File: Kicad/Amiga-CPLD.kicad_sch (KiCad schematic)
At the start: 23 parts, among them CN1 CDTV-DIAG, J1 Conn_01x06_Male, U1 AZ1117-3.3, U2 XC95144XL-TQ100, X1 50MHz

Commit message: PCB: Keep on routing...
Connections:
- net IORDY: now also U2.4 (I/O/GTS2)
- net ~{FLASH_CE}: now also U2.97 (P97)
- net ~{IDE_CS1}: now also U2.2 (I/O/GTS4)
- net ~{IDE_ROMCS}: now also U2.1 (I/O/GTS3)
- net ~{IORD}: now also U2.96 (P96)
- net ~{IOWR}: now also U2.99 (I/O/GSR)
- net ~{I_BUFOE}: now also U2.6 (P6)
- net ~{IDE_CS2}: now reaches U2.3 (I/O/GTS1)
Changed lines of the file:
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@@
   (junction (at 86.995 180.34) (diameter 1.016) (color 0 0 0 0)
   )
-  (no_connect (at 185.42 25.4))
+  (no_connect (at 213.995 32.385))
   (no_connect (at 40.005 39.37))
   (no_connect (at 40.005 44.45))
@@
     (stroke (width 0) (type default) (color 0 0 0 0))
   )
+  (wire (pts (xy 133.35 72.39) (xy 125.095 72.39))
+    (stroke (width 0) (type default) (color 0 0 0 0))
+  )
   (wire (pts (xy 153.67 24.13) (xy 156.21 24.13))
     (stroke (width 0) (type solid) (color 0 0 0 0))
@@
     (stroke (width 0) (type default) (color 0 0 0 0))
   )
-  (wire (pts (xy 249.555 128.27) (xy 257.81 128.27))
-    (stroke (width 0) (type default) (color 0 0 0 0))
-  )
   (wire (pts (xy 81.915 49.53) (xy 86.995 49.53))
     (stroke (width 0) (type default) (color 0 0 0 0))
@@
     (stroke (width 0) (type default) (color 0 0 0 0))
   )
-  (wire (pts (xy 249.555 123.19) (xy 257.81 123.19))
+  (wire (pts (xy 133.35 138.43) (xy 125.095 138.43))
     (stroke (width 0) (type default) (color 0 0 0 0))
   )
@@
     (stroke (width 0) (type default) (color 0 0 0 0))
   )
-  (wire (pts (xy 208.28 27.94) (xy 215.9 27.94))
-    (stroke (width 0) (type default) (color 0 0 0 0))
-  )
   (bus (pts (xy 89.535 69.85) (xy 89.535 72.39))
     (stroke (width 0) (type default) (color 0 0 0 0))
@@
     (stroke (width 0) (type default) (color 0 0 0 0))
   )
-  (wire (pts (xy 249.555 107.95) (xy 257.81 107.95))
+  (wire (pts (xy 133.35 67.31) (xy 125.095 67.31))
     (stroke (width 0) (type default) (color 0 0 0 0))
   )
@@
     (stroke (width 0) (type solid) (color 0 0 0 0))
   )
-  (wire (pts (xy 208.28 20.32) (xy 215.9 20.32))
+  (wire (pts (xy 133.35 140.97) (xy 125.73 140.97))
     (stroke (width 0) (type default) (color 0 0 0 0))
   )
@@
     (stroke (width 0) (type default) (color 0 0 0 0))
   )
-  (wire (pts (xy 249.555 120.65) (xy 257.81 120.65))
+  (wire (pts (xy 133.35 62.23) (xy 125.095 62.23))
     (stroke (width 0) (type default) (color 0 0 0 0))
   )
@@
     (stroke (width 0) (type solid) (color 0 0 0 0))
   )
-  (wire (pts (xy 208.28 17.78) (xy 215.9 17.78))
+  (wire (pts (xy 133.35 64.77) (xy 125.73 64.77))
     (stroke (width 0) (type default) (color 0 0 0 0))
   )
@@
     (stroke (width 0) (type solid) (color 0 0 0 0))
   )
-  (wire (pts (xy 249.555 125.73) (xy 257.81 125.73))
+  (wire (pts (xy 133.35 74.93) (xy 125.095 74.93))
     (stroke (width 0) (type default) (color 0 0 0 0))
   )
@@
     (stroke (width 0) (type solid) (color 0 0 0 0))
   )
-  (wire (pts (xy 249.555 118.11) (xy 257.81 118.11))
-    (stroke (width 0) (type default) (color 0 0 0 0))
-  )
   (wire (pts (xy 113.665 180.34) (xy 122.555 180.34))
     (stroke (width 0) (type solid) (color 0 0 0 0))
@@
     (stroke (width 0) (type solid) (color 0 0 0 0))
   )
-  (wire (pts (xy 208.28 22.86) (xy 215.9 22.86))
-    (stroke (width 0) (type default) (color 0 0 0 0))
-  )
   (wire (pts (xy 29.845 105.41) (xy 40.005 105.41))
     (stroke (width 0) (type default) (color 0 0 0 0))
@@
     (stroke (width 0) (type solid) (color 0 0 0 0))
   )
-  (wire (pts (xy 249.555 110.49) (xy 257.81 110.49))
+  (wire (pts (xy 133.35 69.85) (xy 125.095 69.85))
     (stroke (width 0) (type default) (color 0 0 0 0))
   )
@@
     (effects (font (size 1.27 1.27)) (justify right bottom))
   )
-  (label "~{BGACK}" (at 185.42 15.24 0)
-    (effects (font (size 1.27 1.27)) (justify left bottom))
-  )
   (label "MA9" (at 184.15 31.75 0)
     (effects (font (size 1.27 1.27)) (justify left bottom))
@@
     (effects (font (size 1.27 1.27)) (justify right bottom))
   )
-  (label "~{IDE_CS2}" (at 249.555 107.95 0)
-    (effects (font (size 1.27 1.27)) (justify left bottom))
+  (label "~{IDE_CS2}" (at 133.35 69.85 180)
+    (effects (font (size 1.27 1.27)) (justify right bottom))
   )
   (label "CKE" (at 133.35 100.33 180)
@@
     (effects (font (size 1.27 1.27)) (justify left bottom))
   )
-  (label "RAM_J1" (at 185.42 27.94 0)
+  (label "RAM_J1" (at 212.725 38.1 0)
     (effects (font (size 1.27 1.27)) (justify left bottom))
   )
@@
     (effects (font (size 1.27 1.27)) (justify left bottom))
   )
-  (label "~{IOWR}" (at 249.555 120.65 0)
-    (effects (font (size 1.27 1.27)) (justify left bottom))
+  (label "~{IOWR}" (at 133.35 62.23 180)
+    (effects (font (size 1.27 1.27)) (justify right bottom))
   )
   (label "D6" (at 81.915 102.87 0)
@@
     (effects (font (size 1.27 1.27)) (justify right bottom))
   )
-  (label "~{IDE_IRQ}" (at 249.555 128.27 0)
-    (effects (font (size 1.27 1.27)) (justify left bottom))
-  )
   (label "DQML" (at 130.81 36.83 180)
     (effects (font (size 1.27 1.27)) (justify right bottom))
@@
     (effects (font (size 1.27 1.27)) (justify left bottom))
   )
-  (label "~{INT2}" (at 185.42 17.78 0)
-    (effects (font (size 1.27 1.27)) (justify left bottom))
-  )
   (label "~{AS}" (at 184.15 95.25 0)
     (effects (font (size 1.27 1.27)) (justify left bottom))
@@
     (effects (font (size 1.27 1.27)) (justify left bottom))
   )
-  (label "~{IORD}" (at 249.555 123.19 0)
-    (effects (font (size 1.27 1.27)) (justify left bottom))
+  (label "~{IORD}" (at 133.35 138.43 180)
+    (effects (font (size 1.27 1.27)) (justify right bottom))
   )
   (label "MA11" (at 133.35 110.49 180)
@@
     (effects (font (size 1.27 1.27)) (justify right bottom))
   )
-  (label "IORDY" (at 249.555 125.73 0)
-    (effects (font (size 1.27 1.27)) (justify left bottom))
+  (label "IORDY" (at 133.35 72.39 180)
+    (effects (font (size 1.27 1.27)) (justify right bottom))
   )
   (label "TMS" (at 184.15 148.59 0)
@@
     (effects (font (size 1.27 1.27)) (justify left bottom))
   )
+  (label "~{I_BUFOE}" (at 133.35 74.93 180)
+    (effects (font (size 1.27 1.27)) (justify right bottom))
+  )
   (label "A4" (at 133.35 118.11 180)
     (effects (font (size 1.27 1.27)) (justify right bottom))
@@
     (effects (font (size 1.27 1.27)) (justify left bottom))
   )
-  (label "~{I_BUFOE}" (at 249.555 118.11 0)
-    (effects (font (size 1.27 1.27)) (justify left bottom))
-  )
   (label "D12" (at 184.15 107.95 0)
     (effects (font (size 1.27 1.27)) (justify left bottom))
@@
     (effects (font (size 1.27 1.27)) (justify left bottom))
   )
-  (label "~{IDE_CS1}" (at 249.555 110.49 0)
-    (effects (font (size 1.27 1.27)) (justify left bottom))
+  (label "~{IDE_CS1}" (at 133.35 67.31 180)
+    (effects (font (size 1.27 1.27)) (justify right bottom))
   )
   (label "D13" (at 184.15 105.41 0)
@@
     )
   )
+  (hierarchical_label "~{I_BUFOE}" (shape output) (at 125.095 74.93 180)
+    (effects (font (size 1.27 1.27)) (justify right))
+  )
   (hierarchical_label "BA1" (shape output) (at 125.095 113.03 180)
     (effects (font (size 1.27 1.27)) (justify right))
@@
     (effects (font (size 1.27 1.27)) (justify right))
   )
-  (hierarchical_label "~{FLASH_BSY}" (shape input) (at 215.9 27.94 0)
-    (effects (font (size 1.27 1.27)) (justify left))
-  )
   (hierarchical_label "~{R_BUFOE}" (shape output) (at 193.675 12.7 0)
     (effects (font (size 1.27 1.27)) (justify left))
@@
     (effects (font (size 1.27 1.27)) (justify left))
   )
-  (hierarchical_label "FLASH_A18" (shape output) (at 215.9 22.86 0)
-    (effects (font (size 1.27 1.27)) (justify left))
-  )
-  (hierarchical_label "~{IDE_CS1}" (shape output) (at 257.81 107.95 0)
-    (effects (font (size 1.27 1.27)) (justify left))
+  (hierarchical_label "~{IDE_CS1}" (shape output) (at 125.095 67.31 180)
+    (effects (font (size 1.27 1.27)) (justify right))
   )
   (hierarchical_label "~{CAS}" (shape output) (at 122.555 41.91 180)
     (effects (font (size 1.27 1.27)) (justify right))
   )
-  (hierarchical_label "~{I_BUFOE}" (shape output) (at 257.81 118.11 0)
-    (effects (font (size 1.27 1.27)) (justify left))
-  )
   (hierarchical_label "RAM_~{W}" (shape output) (at 122.555 39.37 180)
     (effects (font (size 1.27 1.27)) (justify right))
   )
-  (hierarchical_label "~{IDE_ROMCS}" (shape output) (at 215.9 17.78 0)
-    (effects (font (size 1.27 1.27)) (justify left))
+  (hierarchical_label "~{IDE_ROMCS}" (shape output) (at 125.73 64.77 180)
+    (effects (font (size 1.27 1.27)) (justify right))
   )
   (hierarchical_label "MA[0..11]" (shape output) (at 264.795 23.495 0)
     (effects (font (size 1.27 1.27)) (justify left))
   )
-  (hierarchical_label "~{FLASH_CE}" (shape output) (at 215.9 20.32 0)
-    (effects (font (size 1.27 1.27)) (justify left))
-  )
-  (hierarchical_label "~{IDE_IRQ}" (shape input) (at 257.81 128.27 0)
-    (effects (font (size 1.27 1.27)) (justify left))
+  (hierarchical_label "~{FLASH_CE}" (shape output) (at 125.73 140.97 180)
+    (effects (font (size 1.27 1.27)) (justify right))
   )
   (hierarchical_label "CKE" (shape output) (at 125.095 100.33 180)
     (effects (font (size 1.27 1.27)) (justify right))
   )
-  (hierarchical_label "~{IDE_CS2}" (shape output) (at 257.81 110.49 0)
-    (effects (font (size 1.27 1.27)) (justify left))
-  )
-  (hierarchical_label "~{IORD}" (shape output) (at 257.81 123.19 0)
-    (effects (font (size 1.27 1.27)) (justify left))
-  )
-  (hierarchical_label "IORDY" (shape input) (at 257.81 125.73 0)
-    (effects (font (size 1.27 1.27)) (justify left))
-  )
-  (hierarchical_label "~{IOWR}" (shape output) (at 257.81 120.65 0)
-    (effects (font (size 1.27 1.27)) (justify left))
+  (hierarchical_label "~{IDE_CS2}" (shape output) (at 125.095 69.85 180)
+    (effects (font (size 1.27 1.27)) (justify right))
+  )
+  (hierarchical_label "~{IORD}" (shape output) (at 125.095 138.43 180)
+    (effects (font (size 1.27 1.27)) (justify right))
+  )
+  (hierarchical_label "IORDY" (shape input) (at 125.095 72.39 180)
+    (effects (font (size 1.27 1.27)) (justify right))
+  )
+  (hierarchical_label "~{IOWR}" (shape output) (at 125.095 62.23 180)
+    (effects (font (size 1.27 1.27)) (justify right))
   )
   (hierarchical_label "BA0" (shape output) (at 125.095 107.95 180)

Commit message: PCB: More routing...
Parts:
- removed JP2: configure_ram, Connector_PinHeader_2.54mm:PinHeader_1x02_P2.54mm_Vertical, symbol Connector:Conn_01x02_Male
- removed R3: 10k, Resistor_SMD:R_0603_1608Metric, symbol Device:R
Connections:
- net BA0: now also U2.29 (P29); no longer U2.32 (P32)
- net BA1: now also U2.32 (P32); no longer U2.34 (P34)
- net CKE: now also U2.27 (I/O/GCK3); no longer U2.28 (P28)
- net DQMH: now also U2.22 (I/O/GCK1)
- net DQML: now also U2.19 (P19)
- net MA0: now also U2.36 (P36); no longer U2.39 (P39)
- net MA1: now also U2.39 (P39); no longer U2.41 (P41)
- net MA10: now also U2.34 (P34); no longer U2.36 (P36)
- net MA11: now also U2.30 (P30); no longer U2.33 (P33)
- net MA2: now also U2.41 (P41); no longer U2.43 (P43)
- net MA3: now also U2.43 (P43); no longer U2.49 (P49)
- net MA8: now also U2.35 (P35); no longer U2.50 (P50)
- net MA9: now also U2.33 (P33); no longer U2.35 (P35)
- net MEMCLK: now also U2.23 (I/O/GCK2); no longer U2.27 (I/O/GCK3)
- net RAM_J1: now also JP3.1 (Pin_1), U2.49 (P49)
- net RAM_~{W}: now also U2.20 (P20)
- net ~{CAS}: now also U2.24 (P24)
- net ~{IDE_OFF}: now also JP1.1 (Pin_1), U2.50 (P50)
- net ~{IDE_ROMCS}: now also U2.99 (I/O/GSR); no longer U2.1 (I/O/GTS3)
- net ~{IOWR}: now also U2.1 (I/O/GTS3); no longer U2.99 (I/O/GSR)
- net ~{RAMCS}: now also U2.28 (P28); no longer U2.30 (P30)
- net ~{RAS}: now also U2.25 (P25); no longer U2.29 (P29)
- net ~{R_BUFOE}: now also U2.18 (P18)
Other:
- moved on the sheet: JP1, JP3

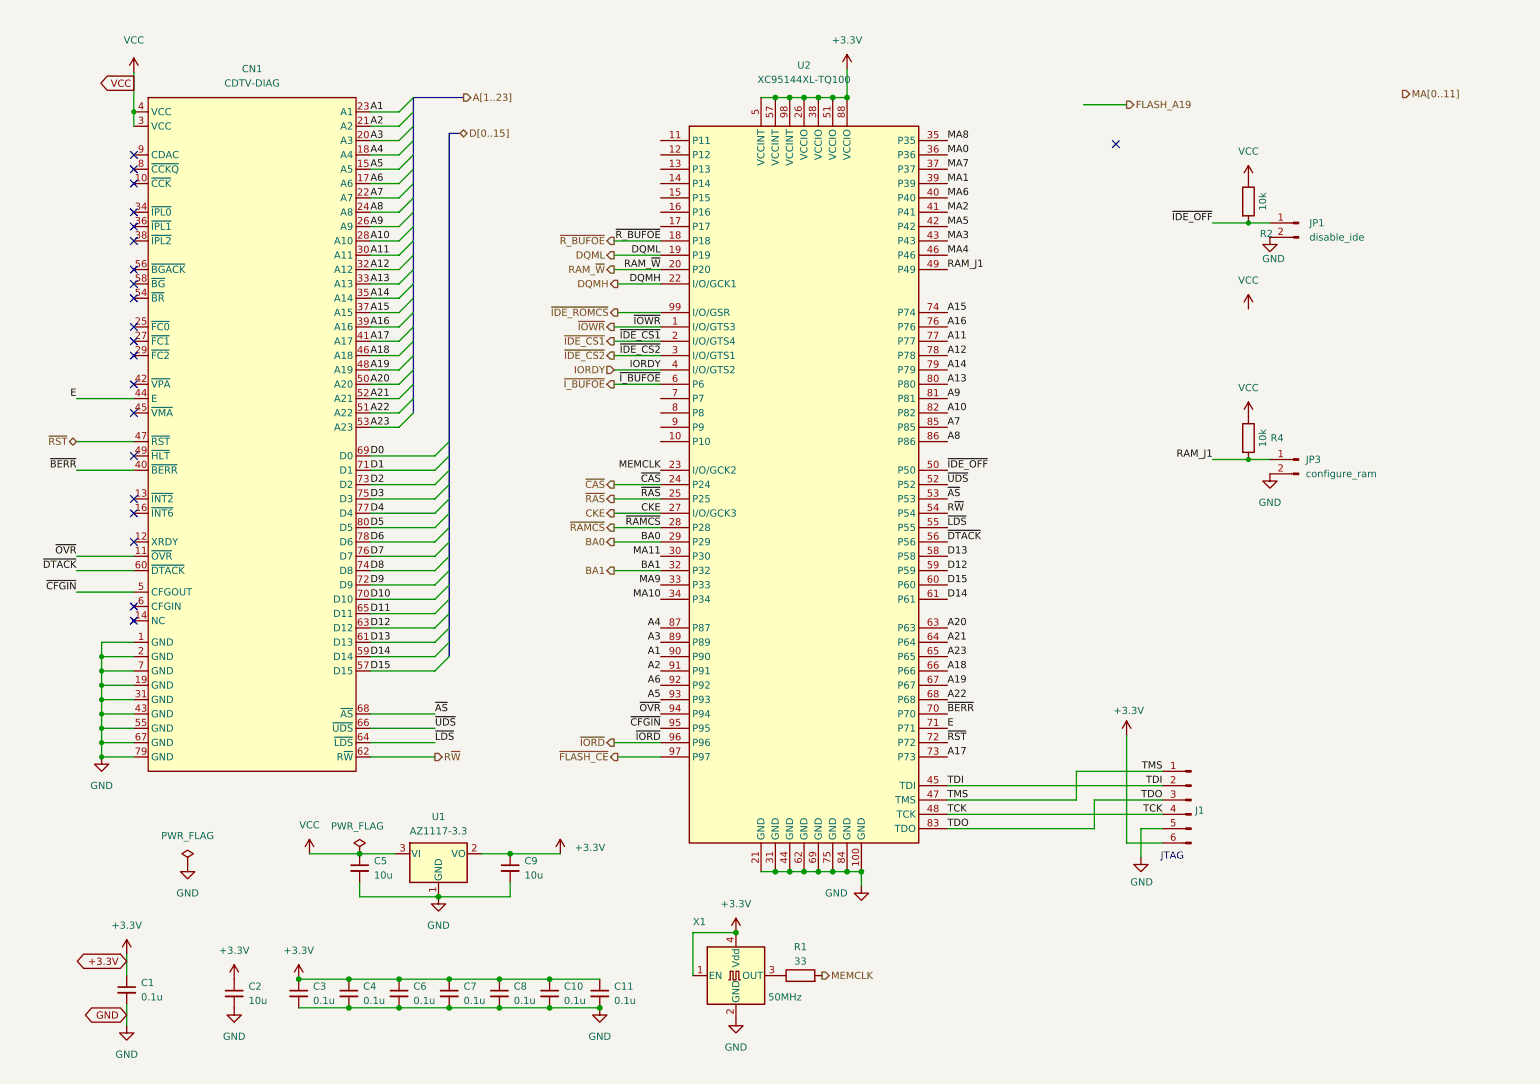
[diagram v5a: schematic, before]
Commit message: PCB: More work...
* Add DIP Switches for Ram/Rom/IDE config
* Route bank select signals for Flash rom
* Flip IDE to bottom of the board
* Add some bulk capacitors
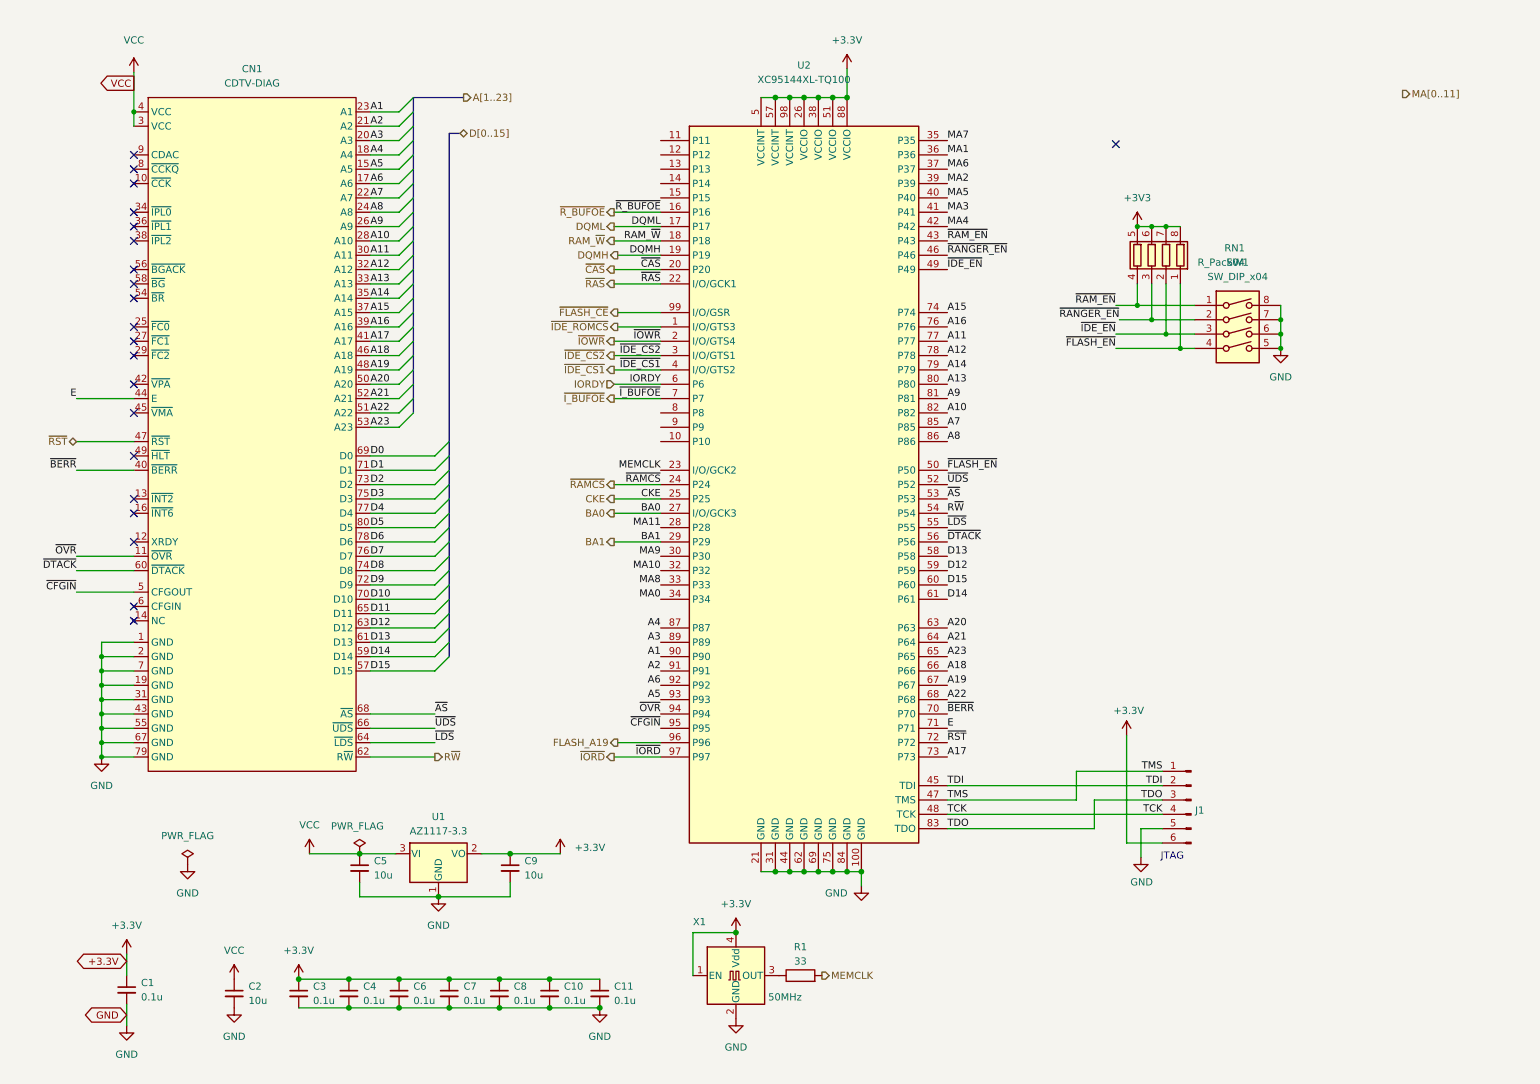
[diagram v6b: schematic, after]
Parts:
- removed JP1: disable_ide, Connector_PinHeader_2.54mm:PinHeader_1x02_P2.54mm_Vertical, symbol Connector:Conn_01x02_Male
- removed JP3: configure_ram, Connector_PinHeader_2.54mm:PinHeader_1x02_P2.54mm_Vertical, symbol Connector:Conn_01x02_Male
- removed R2, R4: 10k, Resistor_SMD:R_0603_1608Metric, symbol Device:R
- added RN1: R_Pack04, Resistor_SMD:R_Array_Convex_4x0603, symbol Device:R_Pack04
- added SW1: SW_DIP_x04, Button_Switch_SMD:SW_DIP_SPSTx04_Slide_Omron_A6H-4101_W6.15mm_P1.27mm, symbol Switch:SW_DIP_x04
- C2: footprint Capacitor_SMD:C_0805_2012Metric_Pad1.18x1.45mm_HandSolder -> Capacitor_Tantalum_SMD:CP_EIA-3216-18_Kemet-A; LCSC # C15850 -> C117023
- J1: value Conn_01x06_Male -> JTAG
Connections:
- net +3V3: now also RN1.5 (R4.2), RN1.6 (R3.2), RN1.7 (R2.2), RN1.8 (R1.2); no longer C2.1
- net BA0: now also U2.27 (I/O/GCK3); no longer U2.29 (P29)
- net BA1: now also U2.29 (P29); no longer U2.32 (P32)
- net CKE: now also U2.25 (P25); no longer U2.27 (I/O/GCK3)
- net DQMH: now also U2.19 (P19); no longer U2.22 (I/O/GCK1)
- net DQML: now also U2.17 (P17); no longer U2.19 (P19)
- net FLASH_A19: now also U2.96 (P96)
- net GND: now also SW1.5, SW1.6, SW1.7, SW1.8
- net IORDY: now also U2.6 (P6); no longer U2.4 (I/O/GTS2)
- net MA0: now also U2.34 (P34); no longer U2.36 (P36)
- net MA1: now also U2.36 (P36); no longer U2.39 (P39)
- net MA10: now also U2.32 (P32); no longer U2.34 (P34)
- net MA11: now also U2.28 (P28); no longer U2.30 (P30)
- net MA2: now also U2.39 (P39); no longer U2.41 (P41)
- net MA3: now also U2.41 (P41); no longer U2.43 (P43)
- net MA4: now also U2.42 (P42); no longer U2.46 (P46)
- net MA5: now also U2.40 (P40); no longer U2.42 (P42)
- net MA6: now also U2.37 (P37); no longer U2.40 (P40)
- net MA7: now also U2.35 (P35); no longer U2.37 (P37)
- net MA8: now also U2.33 (P33); no longer U2.35 (P35)
- net MA9: now also U2.30 (P30); no longer U2.33 (P33)
- net RAM_~{W}: now also U2.18 (P18); no longer U2.20 (P20)
- net VCC: now also C2.1
- net ~{CAS}: now also U2.20 (P20); no longer U2.24 (P24)
- net ~{FLASH_CE}: now also U2.99 (I/O/GSR); no longer U2.97 (P97)
- net ~{IDE_CS1}: now also U2.4 (I/O/GTS2); no longer U2.2 (I/O/GTS4)
- net ~{IDE_ROMCS}: now also U2.1 (I/O/GTS3); no longer U2.99 (I/O/GSR)
- net ~{IORD}: now also U2.97 (P97); no longer U2.96 (P96)
- net ~{IOWR}: now also U2.2 (I/O/GTS4); no longer U2.1 (I/O/GTS3)
- net ~{I_BUFOE}: now also U2.7 (P7); no longer U2.6 (P6)
- net ~{RAMCS}: now also U2.24 (P24); no longer U2.28 (P28)
- net ~{RAS}: now also U2.22 (I/O/GCK1); no longer U2.25 (P25)
- net ~{R_BUFOE}: now also U2.16 (P16); no longer U2.18 (P18)
- net RAM_J1 renamed ~{IDE_EN}
- net ~{IDE_EN}: now also RN1.2 (R2.1), SW1.3
- net ~{IDE_OFF} renamed ~{FLASH_EN}
- net ~{FLASH_EN}: now also RN1.1 (R1.1), SW1.4
- new net ~{RAM_EN}: RN1.4 (R4.1), SW1.1, U2.43 (P43)
- new net ~{RANGER_EN}: RN1.3 (R3.1), SW1.2, U2.46 (P46)
